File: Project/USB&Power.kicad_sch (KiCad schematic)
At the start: 10 parts, among them J2 USB_C sink board 1.3mm, U58 PRTR5V0U2X

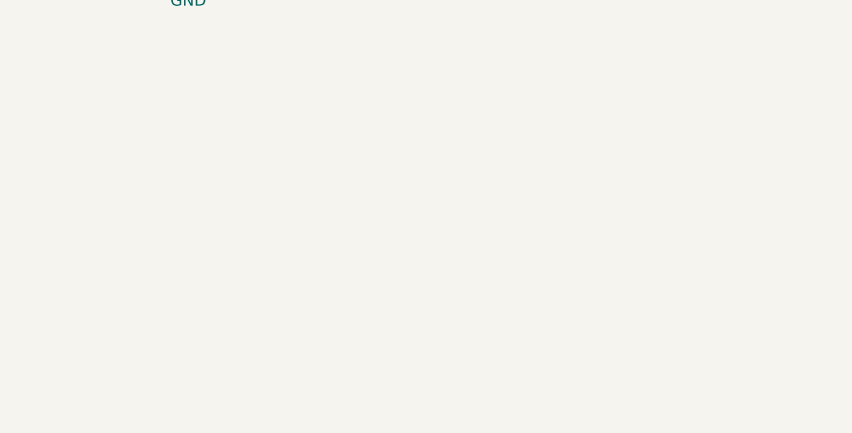
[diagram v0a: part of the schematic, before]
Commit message: created plates and production files for protos
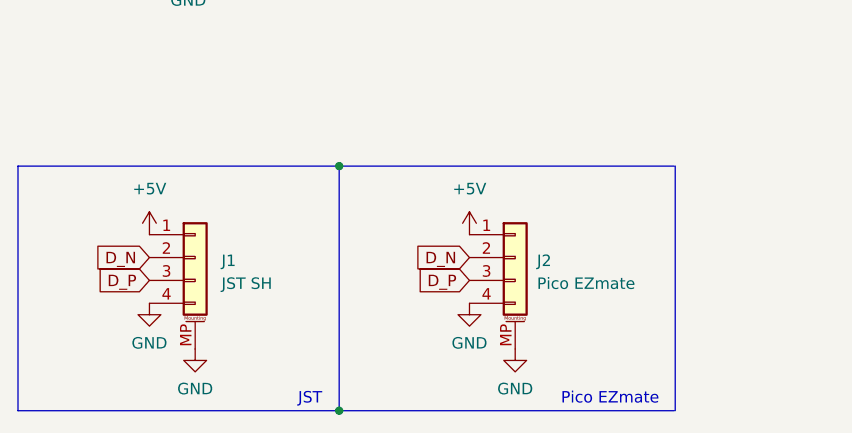
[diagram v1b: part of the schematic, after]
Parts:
- added J1: JST SH, Connector_JST:JST_SH_SM04B-SRSS-TB_1x04-1MP_P1.00mm_Horizontal, symbol Connector_Generic_MountingPin:Conn_01x04_MountingPin
- added J2: Pico EZmate, Connector_Molex:Molex_Pico-EZmate_78171-0004_1x04-1MP_P1.20mm_Vertical, symbol Connector_Generic_MountingPin:Conn_01x04_MountingPin
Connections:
- net +5V: now also J1.1 (Pin_1), J2.1 (Pin_1)
- net D_N: now also J1.2 (Pin_2), J2.2 (Pin_2)
- net D_P: now also J1.3 (Pin_3), J2.3 (Pin_3)
- net GND: now also J1.4 (Pin_4), J1.MP (MountPin), J2.4 (Pin_4), J2.MP (MountPin)
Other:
- note added: "JST"
- note added: "Pico EZmate"

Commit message: pin revision
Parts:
- removed L1: 60R@100MHz, Inductor_SMD:L_1206_3216Metric, symbol Unified-Daughterboard-rescue:L_Core_Ferrite-Device
- added D_PWR1: SMF9.0CA, Diode_SMD:D_SOD-123, symbol Device:D_TVS
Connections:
- net +5V: now also D_PWR1.1 (A1)
- net GND: now also D_PWR1.2 (A2)
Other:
- moved on the sheet: C?, F2, U58

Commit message: update
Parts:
- F2: value ASMD1206-150 -> 500mA; LCSC C135341 -> C70076
- renumbered J2 to J12

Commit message: revision work
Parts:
- added U64: AP2112K-3.3, Package_TO_SOT_SMD:SOT-23-5, symbol Regulator_Linear:AP2112K-3.3
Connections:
- net +3V3: now also U64.5 (VOUT); no longer U?.2 (VO)
- net +5V: now also U64.1 (VIN); no longer U?.3 (VI)
- net GND: now also U64.2 (GND), U64.3 (EN); no longer U?.1 (GND)
- no-connect marks 2 -> 3
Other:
- note added: "CHECK ON AP2112 third pin"
- moved on the sheet: U?
